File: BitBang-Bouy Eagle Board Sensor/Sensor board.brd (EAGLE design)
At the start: 33 x 14.9 mm, 4 parts

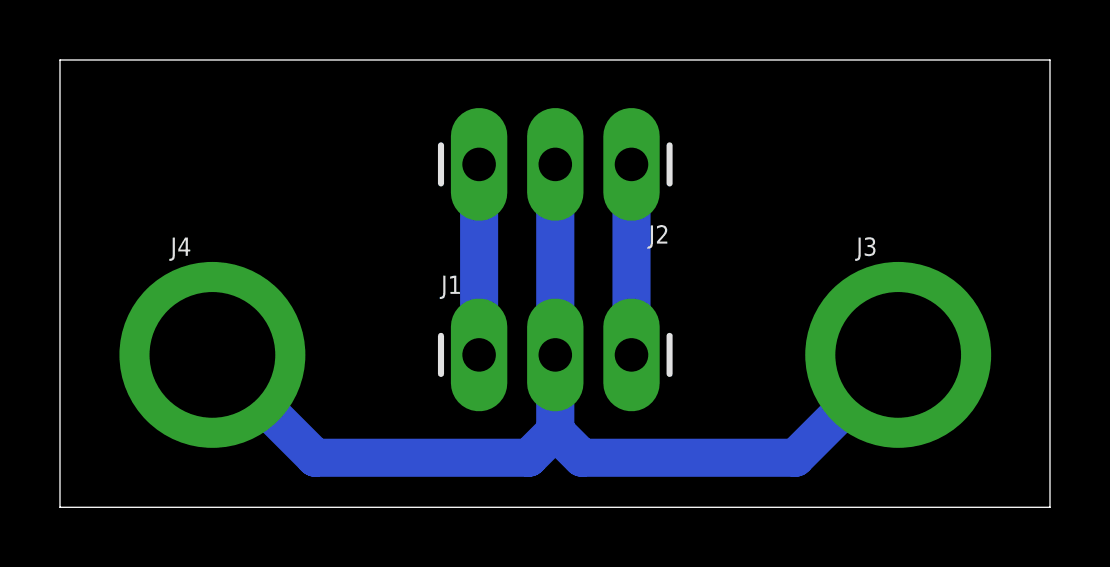
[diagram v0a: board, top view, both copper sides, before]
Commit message: Trascient detector added
A trascient detector added in order to read mor accurately the hall sensor, it uses a registry ring and a window lecture
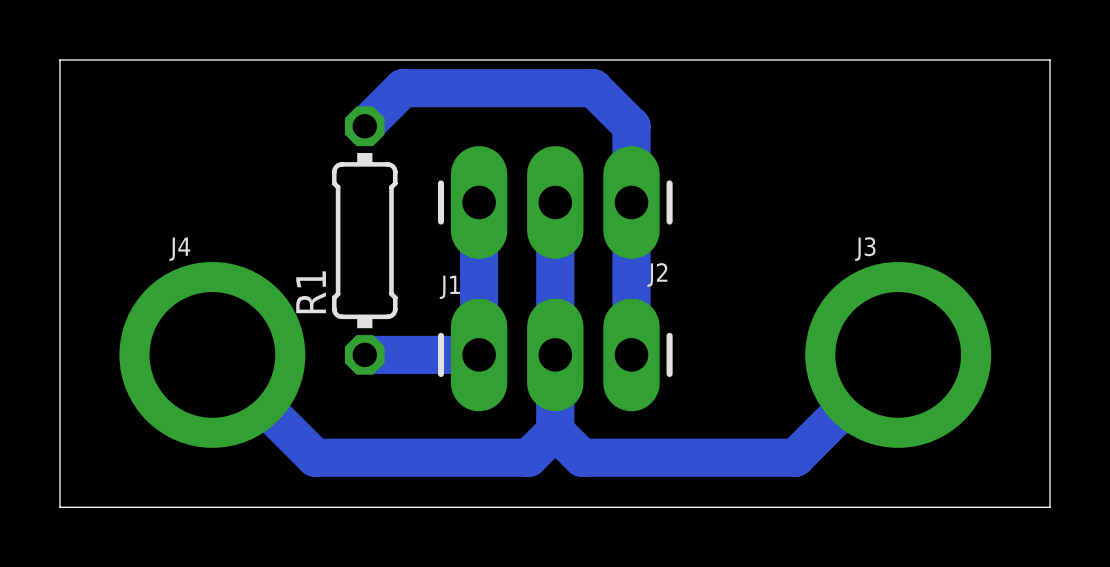
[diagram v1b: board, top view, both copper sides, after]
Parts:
- added R1: (no value), rcl:0204/7
- moved J2 1.27 mm to (19.1, 10.2)
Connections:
- net N$1: now also R1.2
- net N$3: now also R1.1
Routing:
- net N$1: track 6.35 -> 17.6 mm
- net N$3: track 6.35 -> 8.89 mm
- net N$2: track 35.3 -> 34.1 mm
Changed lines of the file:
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@@
 <?xml version="1.0" encoding="utf-8"?>
 <!DOCTYPE eagle SYSTEM "eagle.dtd">
-<eagle version="8.6.3">
+<eagle version="9.1.0">
 <drawing>
 <settings>
@@
 <param name="checkStop" value="0"/>
 <param name="checkValues" value="0"/>
+<param name="checkNames" value="1"/>
+<param name="checkWireStubs" value="1"/>
+<param name="checkPolygonWidth" value="0"/>
 <param name="useDiameter" value="13"/>
 <param name="maxErrors" value="50"/>
@@
 <elements>
 <element name="J1" library="SparkFun-Connectors" package="1X03_LONGPADS" value="" x="13.97" y="5.08"/>
-<element name="J2" library="SparkFun-Connectors" package="1X03_LONGPADS" value="" x="19.05" y="11.43" rot="R180"/>
+<element name="J2" library="SparkFun-Connectors" package="1X03_LONGPADS" value="" x="19.05" y="10.16" rot="R180"/>
 <element name="J3" library="SparkFun-Connectors" package="SMTSO-256-ET-0.165DIA" value="" x="27.94" y="5.08">
 <attribute name="PROD_ID" value="HW-08694" x="27.94" y="5.08" size="1.778" layer="27" display="off"/>
@@
 <attribute name="PROD_ID" value="HW-08694" x="5.08" y="5.08" size="1.778" layer="27" display="off"/>
 </element>
+<element name="R1" library="rcl" library_urn="urn:adsk.eagle:library:334" package="0204/7" package3d_urn="urn:adsk.eagle:package:23498/1" value="" x="10.16" y="8.89" rot="R90">
+<attribute name="SPICEPREFIX" value="R" x="10.16" y="8.89" size="1.778" layer="27" rot="R90" display="off"/>
+</element>
 </elements>
 <signals>
@@
 <contactref element="J1" pad="3"/>
 <contactref element="J2" pad="1"/>
-<wire x1="19.05" y1="5.08" x2="19.05" y2="11.43" width="1.27" layer="16"/>
+<wire x1="19.05" y1="5.08" x2="19.05" y2="10.16" width="1.27" layer="16"/>
+<contactref element="R1" pad="2"/>
+<wire x1="10.16" y1="12.7" x2="11.43" y2="13.97" width="1.27" layer="16"/>
+<wire x1="11.43" y1="13.97" x2="17.78" y2="13.97" width="1.27" layer="16"/>
+<wire x1="17.78" y1="13.97" x2="19.05" y2="12.7" width="1.27" layer="16"/>
+<wire x1="19.05" y1="12.7" x2="19.05" y2="10.16" width="1.27" layer="16"/>
 </signal>
 <signal name="N$2">
@@
 <contactref element="J4" pad="P$1"/>
 <contactref element="J3" pad="P$1"/>
-<wire x1="16.51" y1="5.08" x2="16.51" y2="11.43" width="1.27" layer="16"/>
+<wire x1="16.51" y1="5.08" x2="16.51" y2="10.16" width="1.27" layer="16"/>
 <wire x1="16.51" y1="5.08" x2="16.51" y2="2.54" width="1.27" layer="16"/>
 <wire x1="16.51" y1="2.54" x2="15.621" y2="1.651" width="1.27" layer="16"/>
@@
 <contactref element="J1" pad="1"/>
 <contactref element="J2" pad="3"/>
-<wire x1="13.97" y1="5.08" x2="13.97" y2="11.43" width="1.27" layer="16"/>
+<wire x1="13.97" y1="5.08" x2="13.97" y2="10.16" width="1.27" layer="16"/>
+<contactref element="R1" pad="1"/>
+<wire x1="13.97" y1="5.08" x2="10.16" y2="5.08" width="1.27" layer="16"/>
 </signal>
 </signals>
+<mfgpreviewcolors>
+<mfgpreviewcolor name="soldermaskcolor" color="0xC8008000"/>
+<mfgpreviewcolor name="silkscreencolor" color="0xFFFEFEFE"/>
+<mfgpreviewcolor name="backgroundcolor" color="0xFF282828"/>
+<mfgpreviewcolor name="coppercolor" color="0xFFFFBF00"/>
+<mfgpreviewcolor name="substratecolor" color="0xFF786E46"/>
+</mfgpreviewcolors>
 </board>
 </drawing>
+<compatibility>
+<note version="8.2" severity="warning">
+Since Version 8.2, EAGLE supports online libraries. The ids
+of those online libraries will not be understood (or retained)
+with this version.
+</note>
+<note version="8.3" severity="warning">
+Since Version 8.3, EAGLE supports URNs for individual library
+assets (packages, symbols, and devices). The URNs of those assets
+will not be understood (or retained) with this version.
+</note>
+<note version="8.3" severity="warning">
+Since Version 8.3, EAGLE supports the association of 3D packages
+with devices in libraries, schematics, and board files. Those 3D
+packages will not be understood (or retained) with this version.
+</note>
+</compatibility>
 </eagle>
